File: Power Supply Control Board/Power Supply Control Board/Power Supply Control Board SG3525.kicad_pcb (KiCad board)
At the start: 2 copper layers, 49.8 x 49.8 mm, 52 parts, among them J1 Conn_01x14_Male, Q1 BC546, Q2 BC546, Q3 MPSA92, U1 LM393, U2 SG3525, U3 IR2110

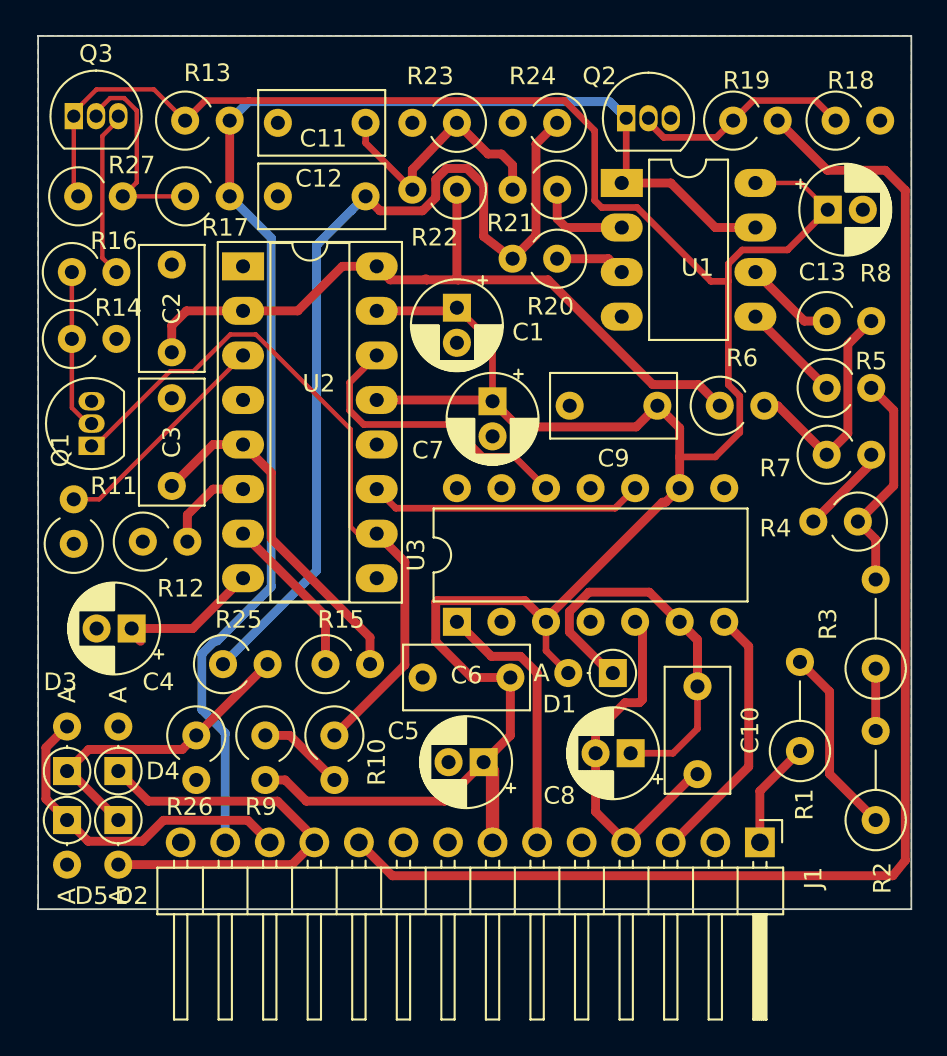
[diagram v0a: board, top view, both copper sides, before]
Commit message: Finish design of SG3525 Board into SMD
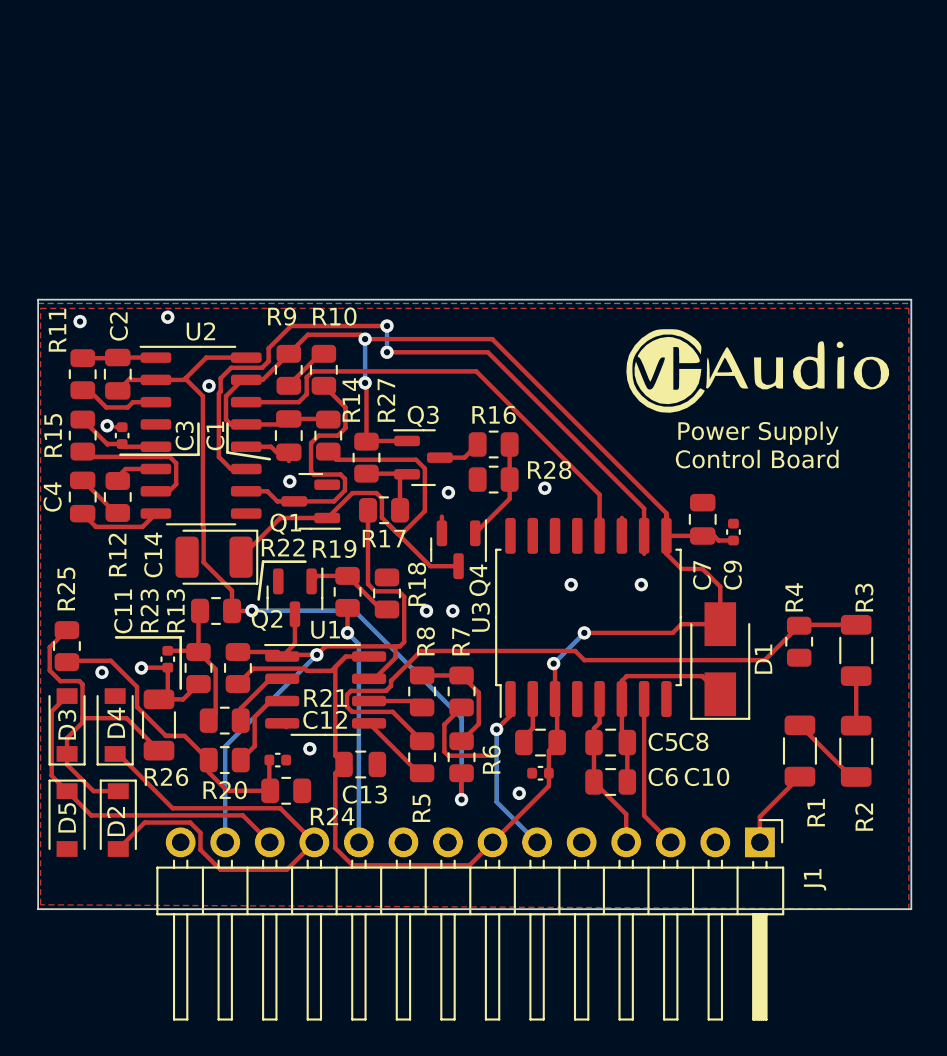
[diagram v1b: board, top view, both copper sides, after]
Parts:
- added C14: 100µ/6.3V, Capacitor_Tantalum_SMD:CP_EIA-3528-21_Kemet-B, F.Cu at (112.1, 106.9)
- added Q4: MMBT5551L, Package_TO_SOT_SMD:SOT-23, F.Cu at (126.1, 106.5)
- added R28: 10k, Resistor_SMD:R_0805_2012Metric, F.Cu at (128.1, 102.5)
- added REF**: VHAudio_Logo_15mm, LogoLibrary:VHAudio_Logo_15mm, F.Cu at (143.1, 96.3)
- C1, C13, C4, C5, C7, C8: footprint Capacitor_THT:CP_Radial_D5.0mm_P2.00mm -> Capacitor_SMD:C_0805_2012Metric
- C10, C2: footprint Capacitor_THT:C_Rect_L7.0mm_W3.5mm_P5.00mm -> Capacitor_SMD:C_0805_2012Metric
- C11, C12, C3, C6, C9: footprint Capacitor_THT:C_Rect_L7.0mm_W3.5mm_P5.00mm -> Capacitor_SMD:C_0402_1005Metric
- D1: value MURS120 -> US1MG; footprint Diode_THT:D_DO-35_SOD27_P2.54mm_Vertical_AnodeUp -> Diode_SMD:D_SMA
- D2, D3, D4, D5: footprint Diode_THT:D_DO-35_SOD27_P2.54mm_Vertical_AnodeUp -> Diode_SMD:D_SOD-123
- Q1, Q2: value BC546 -> MMBT5551L; footprint Package_TO_SOT_THT:TO-92_Inline -> Package_TO_SOT_SMD:SOT-23
- Q3: value MPSA92 -> MMBT5401; footprint Package_TO_SOT_THT:TO-92_Inline -> Package_TO_SOT_SMD:SOT-23
- R1, R2, R3: value 150k 0.5W -> 100k 0.5W; footprint Resistor_THT:R_Axial_DIN0309_L9.0mm_D3.2mm_P5.08mm_Vertical -> Resistor_SMD:R_1206_3216Metric
- R10, R11, R12, R13, R15, R17, R18, R19, R20, R21, R22, R23, R24, R25, R27, R5, R6, R7, R8, R9: footprint Resistor_THT:R_Axial_DIN0309_L9.0mm_D3.2mm_P2.54mm_Vertical -> Resistor_SMD:R_0805_2012Metric
- R14: value 10k -> 22k; footprint Resistor_THT:R_Axial_DIN0309_L9.0mm_D3.2mm_P2.54mm_Vertical -> Resistor_SMD:R_0805_2012Metric
- R16: value 10k -> 47k; footprint Resistor_THT:R_Axial_DIN0309_L9.0mm_D3.2mm_P2.54mm_Vertical -> Resistor_SMD:R_0805_2012Metric
- R26: footprint Resistor_THT:R_Axial_DIN0309_L9.0mm_D3.2mm_P2.54mm_Vertical -> Resistor_SMD:R_1206_3216Metric
- R4: value 12k -> 2k7; footprint Resistor_THT:R_Axial_DIN0309_L9.0mm_D3.2mm_P2.54mm_Vertical -> Resistor_SMD:R_0805_2012Metric
- U1: footprint Package_DIP:DIP-8_W7.62mm_LongPads -> Package_SO:SOIC-8_3.9x4.9mm_P1.27mm
- U2: footprint Package_DIP:DIP-16_W7.62mm_Socket_LongPads -> Package_SO:SO-16_3.9x9.9mm_P1.27mm
- U3: footprint Package_DIP:DIP-14_W7.62mm -> Package_SO:SOIC-16W_7.5x10.3mm_P1.27mm
- moved C13 41.3 mm to (120.5, 118.8)
- moved R24 41.1 mm to (116.2, 120.2), turned to 0 degrees
- moved R18 37.2 mm to (122.0, 109.0), turned to 90 degrees
- moved R21 35.7 mm to (112.8, 116.2)
- moved R19 34.7 mm to (119.8, 108.9), turned to -90 degrees
- moved R23 34.4 mm to (111.2, 113.2), turned to -90 degrees
- moved R20 34.3 mm to (112.8, 118.5)
- moved U1 33.5 mm to (118.5, 114.5)
- moved Q2 33.2 mm to (116.8, 109.2), turned to -90 degrees
- moved C11 32.6 mm to (109.5, 112.8), turned to -90 degrees
- moved C12 32.5 mm to (115.8, 118.5), turned to 0 degrees
- moved R13 31.4 mm to (113.5, 113.2), turned to 90 degrees
- moved R8 31.3 mm to (124.0, 114.6), turned to 90 degrees
- moved R5 31.2 mm to (124.0, 118.3), turned to 90 degrees
- moved Q3 27.9 mm to (124.1, 101.3)
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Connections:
- Q1 pad 1: Net-(Q1-Pad1) -> Net-(C14-Pad1)
- Q1 pad 2: Net-(Q1-Pad2) -> GND
- Q1 pad 3: GND -> Net-(Q1-Pad3)
- Q2 pad 1: ~ShutDown -> Net-(Q2-Pad1)
- Q2 pad 2: Net-(Q2-Pad2) -> GND
- Q2 pad 3: GND -> ~ShutDown
- R10 pad 1: Net-(Q1-Pad1) -> Net-(Q1-Pad3)
- R14 pad 1: Net-(Q1-Pad2) -> +16V
- R14 pad 2: GND -> Net-(C14-Pad1)
- R16 pad 1: Net-(Q1-Pad2) -> Net-(Q3-Pad3)
- R16 pad 2: Net-(Q3-Pad3) -> Net-(Q4-Pad1)
- R18 pad 1: Net-(Q2-Pad2) -> Net-(Q2-Pad1)
- R19 pad 1: Net-(Q2-Pad2) -> Net-(Q2-Pad1)
- U2 pad 10: Net-(Q1-Pad1) -> Net-(Q1-Pad3)
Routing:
- net ShutDown: track 79.5 -> 13.6 mm, vias 0 -> 1
- net +16V: track 162.7 -> 111.7 mm, vias 0 -> 4
- net ~ShutDown: track 80.1 -> 37.0 mm, vias 0 -> 1
- net Net-(Q1-Pad1): track 40.7 -> 0.00 mm
- net Net-(C12-Pad1): track 52.9 -> 17.8 mm
- net Net-(C14-Pad1): track 0.00 -> 27.7 mm
- net Net-(R3-Pad2): track 12.7 -> 37.1 mm
- net Net-(U2-Pad11): track 15.7 -> 40.0 mm, vias 0 -> 2
- net GND: track 5.18 -> 26.8 mm, vias 0 -> 15
- net Net-(Q1-Pad3): track 0.00 -> 16.2 mm
- net Net-(C3-Pad1): track 20.6 -> 4.83 mm
- net Net-(C10-Pad1): track 27.0 -> 12.0 mm
- net Net-(Q2-Pad2): track 12.8 -> 0.00 mm
- net Vs: track 21.3 -> 9.07 mm
- net Net-(U2-Pad14): track 16.8 -> 27.7 mm
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- added copper zone on F.Cu, net GND
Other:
- board size 49.8 x 49.8 mm -> 49.8 x 34.8 mm
- rule pad_to_mask_clearance: 0.0762 -> 0.05
- board text added: "+16 V"
- board text added: "CS +"
- board text added: "CS -"
- board text added: "GND"
- board text added: "Ho"
- board text added: "JLCJLCJLCJLC"
- board text added: "Lo"
- board text added: "Power Supply Control Board"
- board text added: "Shd"
- board text added: "Vb+"
- board text added: "Vs"
- board text added: "X"
- board text added: "~Shd"
